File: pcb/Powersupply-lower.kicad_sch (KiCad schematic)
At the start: 0 parts

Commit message: pcp lower switcher made & implemented
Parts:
- added U3: TPS54294PWP, PWP16_2P31X2P46, symbol TPS54294:TPS54294PWP
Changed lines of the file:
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@@
 	(generator_version "10.0")
 	(paper "A4")
+	(symbol
+		(lib_id "TPS54294:TPS54294PWP")
+		(at 97.79 123.19 0)
+		(unit 1)
+		(body_style 1)
+		(exclude_from_sim no)
+		(in_bom yes)
+		(on_board yes)
+		(in_pos_files yes)
+		(dnp no)
+		(fields_autoplaced yes)
+		(property "Reference" "U3"
+			(at 139.7 62.23 0)
+			(show_name no)
+			(do_not_autoplace no)
+			(effects
+				(font
+					(size 1.524 1.524)
+				)
+			)
+		)
+		(property "Value" "TPS54294PWP"
+			(at 139.7 64.77 0)
+			(show_name no)
+			(do_not_autoplace no)
+			(effects
+				(font
+					(size 1.524 1.524)
+				)
+			)
+		)
+		(property "Footprint" "PWP16_2P31X2P46"
+			(at 138.684 100.584 0)
+			(hide yes)
+			(show_name no)
+			(do_not_autoplace no)
+			(effects
+				(font
+					(size 1.27 1.27)
+					(italic yes)
+				)
+			)
+		)
+		(property "Datasheet" "https://www.ti.com/lit/gpn/tps54294"
+			(at 138.43 96.774 0)
+			(hide yes)
+			(show_name no)
+			(do_not_autoplace no)
+			(effects
+				(font
+					(size 1.27 1.27)
+					(italic yes)
+				)
+			)
+		)
+		(property "Description" ""
+			(at 97.79 123.19 0)
+			(hide yes)
+			(show_name no)
+			(do_not_autoplace no)
+			(effects
+				(font
+					(size 1.27 1.27)
+				)
+			)
+		)
+		(pin "11"
+		)
+		(pin "3"
+		)
+		(pin "7"
+		)
+		(pin "2"
+		)
+		(pin "5"
+		)
+		(pin "1"
+		)
+		(pin "4"
+		)
+		(pin "6"
+		)
+		(pin "10"
+		)
+		(pin "9"
+		)
+		(pin "8"
+		)
+		(pin "15"
+		)
+		(pin "12"
+		)
+		(pin "16"
+		)
+		(pin "13"
+		)
+		(pin "14"
+		)
+		(instances
+			(project "tdt4295"
+				(path "/603dd496-f9c4-4a31-9104-19eec41ebc98/634870db-7705-458e-b29f-8b3e7772e7aa/a39ac6f6-156d-4e0b-9cc4-d1c3d15eb944"
+					(reference "U3")
+					(unit 1)
+				)
+			)
+		)
+	)
 )

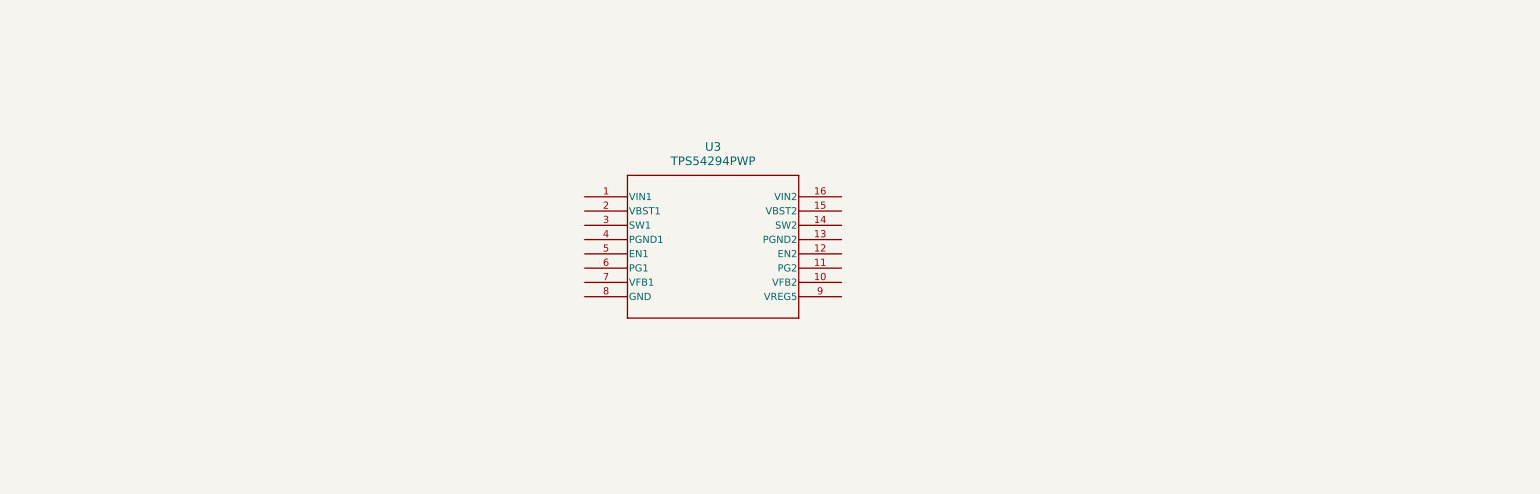
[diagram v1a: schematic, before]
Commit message: pcp lower made
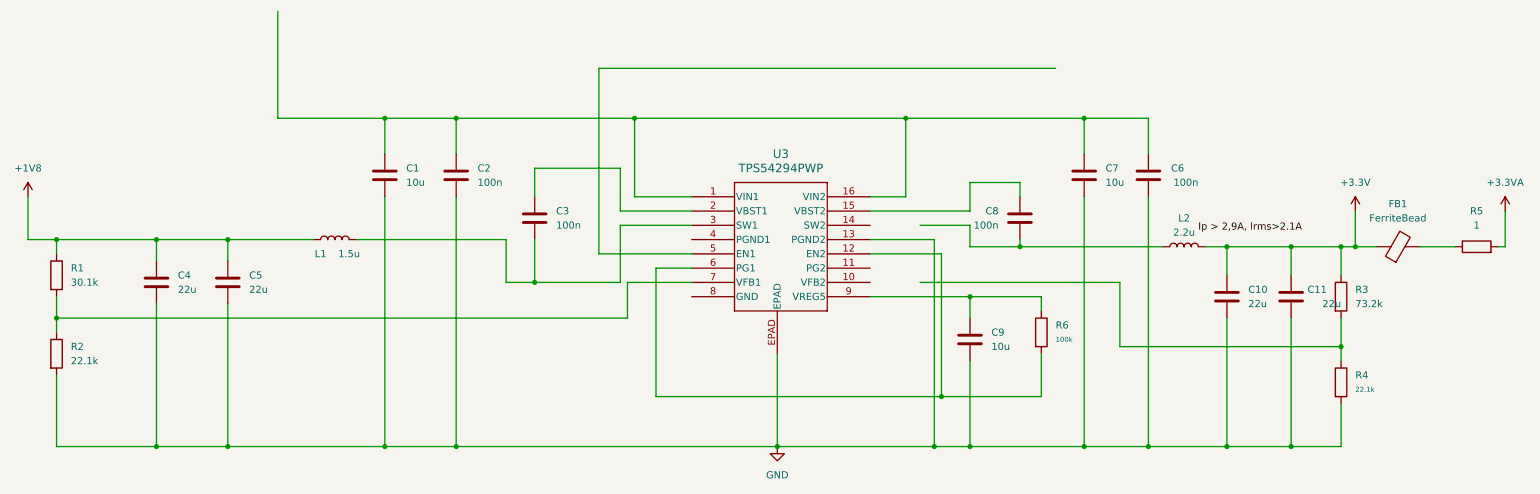
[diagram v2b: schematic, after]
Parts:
- removed U3: TPS54294PWP, PWP16_2P31X2P46, symbol TPS54294:TPS54294PWP
- added C1, C7, C9: 10u, symbol Device:C
- added C10, C11, C4, C5: 22u, symbol Device:C
- added C2, C3, C6, C8: 100n, symbol Device:C
- added FB1: FerriteBead, symbol Device:FerriteBead
- added L1: 1.5u, Relay_THT:Relay_DPDT_Kemet_EC2_NU_DoubleCoil, symbol Device:L
- added L2: 2.2u, Relay_THT:Relay_DPDT_Kemet_EC2_NU_DoubleCoil, symbol Device:L
- added R1: 30.1k, symbol Device:R
- added R2, R4: 22.1k, symbol Device:R
- added R3: 73.2k, symbol Device:R
- added R5: 1, symbol Device:R
- added R6: 100k, symbol Device:R
- added U3: TPS54294PWP, PWP16_2P31X2P46, symbol TPS54294PWP:TPS54294PWP
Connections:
- new net: FB1.2, R5.1
- new net: C1.1, C2.1, C6.1, C7.1, U3.1 (VIN1), U3.16 (VIN2)
- new net: C9.1, R6.1, U3.9 (VREG5)
- new net: R6.2, U3.12 (EN2), U3.6 (PG1)
- new net: R3.2, R4.1
- new net: R1.2, R2.1, U3.7 (VFB1)
- new net: C3.1, U3.2 (VBST1)
- new net: C3.2, L1.2, U3.3 (SW1)
- new net: C8.1, U3.15 (VBST2)
- new net: C8.2, L2.1
- new net +1V8: C4.1, C5.1, L1.1, R1.1
- new net +3.3V: C10.1, C11.1, FB1.1, L2.2, R3.1
- new net +3.3VA: R5.2
- new net GND: C1.2, C10.2, C11.2, C2.2, C4.2, C5.2, C6.2, C7.2, C9.2, R2.2, R4.2, U3.13 (PGND2), U3.EPAD

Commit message: fixed unconnected wire and some readability
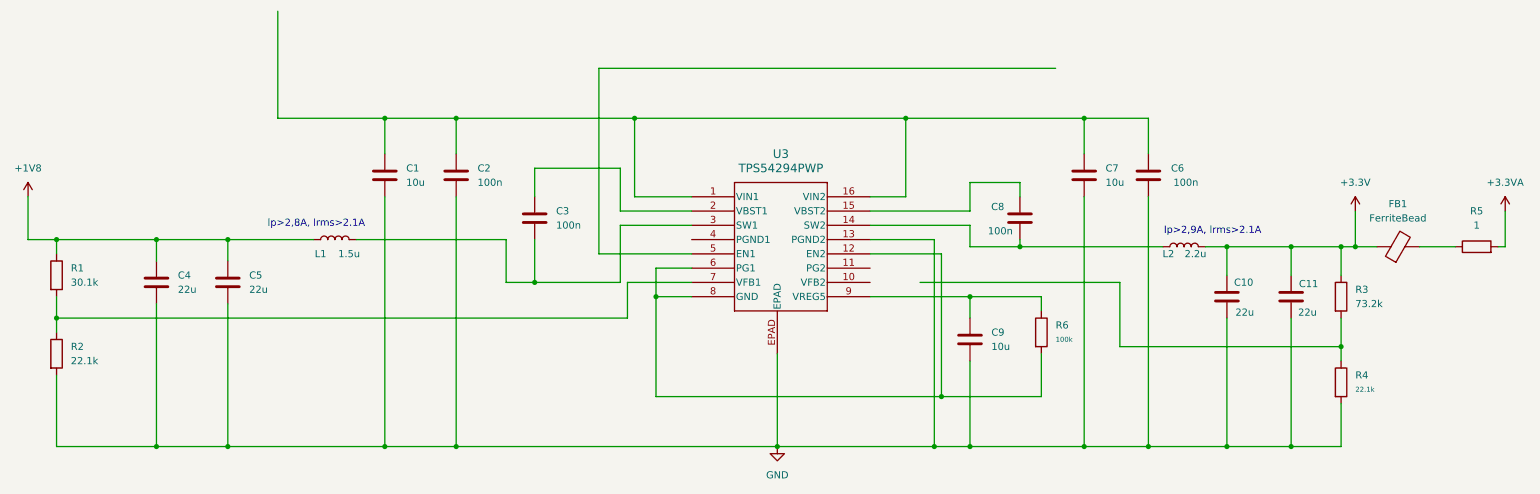
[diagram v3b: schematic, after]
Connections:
- net at R6.2, U3.12 (EN2), U3.6 (PG1): now also U3.8 (GND)
- net at C8.2, L2.1: now also U3.14 (SW2)
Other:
- note added: "lp>2,8A, lrms>2.1A"
- note added: "lp>2,9A, lrms>2.1A"
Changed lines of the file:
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@@
 	(generator_version "10.0")
 	(paper "A4")
+	(text "lp>2,9A, lrms>2.1A"
+		(exclude_from_sim no)
+		(at 228.6 77.216 0)
+		(effects
+			(font
+				(size 1.27 1.27)
+			)
+		)
+	)
+	(text "lp>2,8A, lrms>2.1A"
+		(exclude_from_sim no)
+		(at 69.088 75.946 0)
+		(effects
+			(font
+				(size 1.27 1.27)
+			)
+		)
+	)
 	(junction
 		(at 231.14 115.57)
@@
 	)
 	(junction
+		(at 129.54 88.9)
+		(diameter 0)
+		(color 0 0 0 0)
+	)
+	(junction
 		(at 251.46 80.01)
 		(diameter 0)
@@
 	(wire
 		(pts
-			(xy 176.53 76.2) (xy 185.42 76.2)
-		)
-		(stroke
-			(width 0)
-			(type default)
-		)
-	)
-	(wire
-		(pts
 			(xy 198.12 88.9) (xy 198.12 91.44)
 		)
@@
 	(wire
 		(pts
+			(xy 129.54 88.9) (xy 135.89 88.9)
+		)
+		(stroke
+			(width 0)
+			(type default)
+		)
+	)
+	(wire
+		(pts
 			(xy 22.86 115.57) (xy 40.64 115.57)
 		)
@@
 	(wire
 		(pts
-			(xy 129.54 83.82) (xy 129.54 106.68)
+			(xy 129.54 83.82) (xy 129.54 88.9)
 		)
 		(stroke
@@
 	(wire
 		(pts
+			(xy 129.54 88.9) (xy 129.54 106.68)
+		)
+		(stroke
+			(width 0)
+			(type default)
+		)
+	)
+	(wire
+		(pts
 			(xy 123.19 76.2) (xy 135.89 76.2)
 		)
@@
 	(wire
 		(pts
-			(xy 22.86 102.87) (xy 22.86 115.57)
+			(xy 167.64 76.2) (xy 185.42 76.2)
 		)
 		(stroke
@@
 		)
 	)
-	(label "lp > 2,9A, lrms>2.1A"
-		(at 226.06 77.47 0)
-		(effects
-			(font
-				(size 1.27 1.27)
-			)
-			(justify left bottom)
+	(wire
+		(pts
+			(xy 22.86 102.87) (xy 22.86 115.57)
+		)
+		(stroke
+			(width 0)
+			(type default)
 		)
 	)
@@
 		(in_pos_files yes)
 		(dnp no)
-		(fields_autoplaced yes)
 		(property "Reference" "C10"
-			(at 234.95 87.6299 0)
+			(at 232.41 86.36 0)
 			(show_name no)
 			(do_not_autoplace no)
@@
 		)
 		(property "Value" "22u"
-			(at 234.95 90.1699 0)
+			(at 232.664 91.694 0)
 			(show_name no)
 			(do_not_autoplace no)
@@
 		(in_pos_files yes)
 		(dnp no)
-		(fields_autoplaced yes)
 		(property "Reference" "C8"
-			(at 190.5 73.6599 0)
+			(at 191.516 72.898 0)
 			(show_name no)
 			(do_not_autoplace no)
@@
 		)
 		(property "Value" "100n"
-			(at 190.5 76.1999 0)
+			(at 193.04 77.216 0)
 			(show_name no)
 			(do_not_autoplace no)
@@
 		(dnp no)
 		(property "Reference" "C11"
-			(at 248.92 87.63 0)
+			(at 247.396 86.614 0)
 			(show_name no)
 			(do_not_autoplace no)
@@
 		)
 		(property "Value" "22u"
-			(at 251.46 90.17 0)
+			(at 247.142 91.694 0)
 			(show_name no)
 			(do_not_autoplace no)
@@
 		(in_pos_files yes)
 		(dnp no)
-		(fields_autoplaced yes)
 		(property "Reference" "L2"
-			(at 223.52 74.93 90)
+			(at 220.726 81.28 90)
 			(show_name no)
 			(do_not_autoplace no)
@@
 		)
 		(property "Value" "2.2u"
-			(at 223.52 77.47 90)
+			(at 225.552 81.28 90)
 			(show_name no)
 			(do_not_autoplace no)

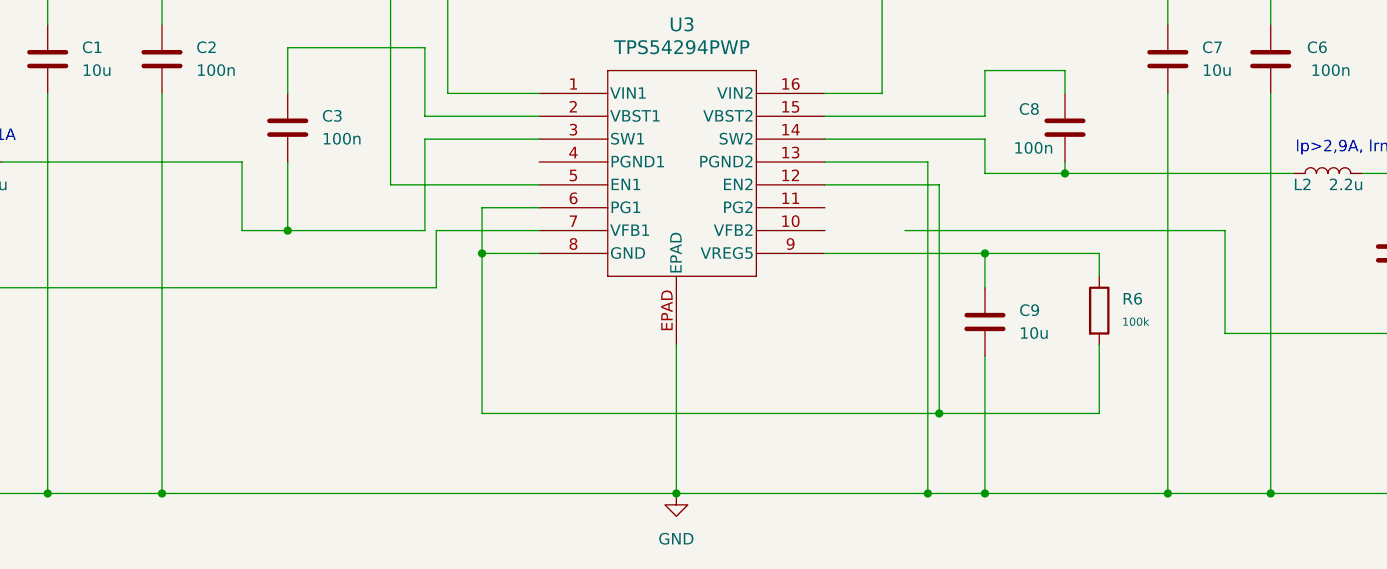
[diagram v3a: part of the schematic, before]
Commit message: (psp) fixed wrong wires
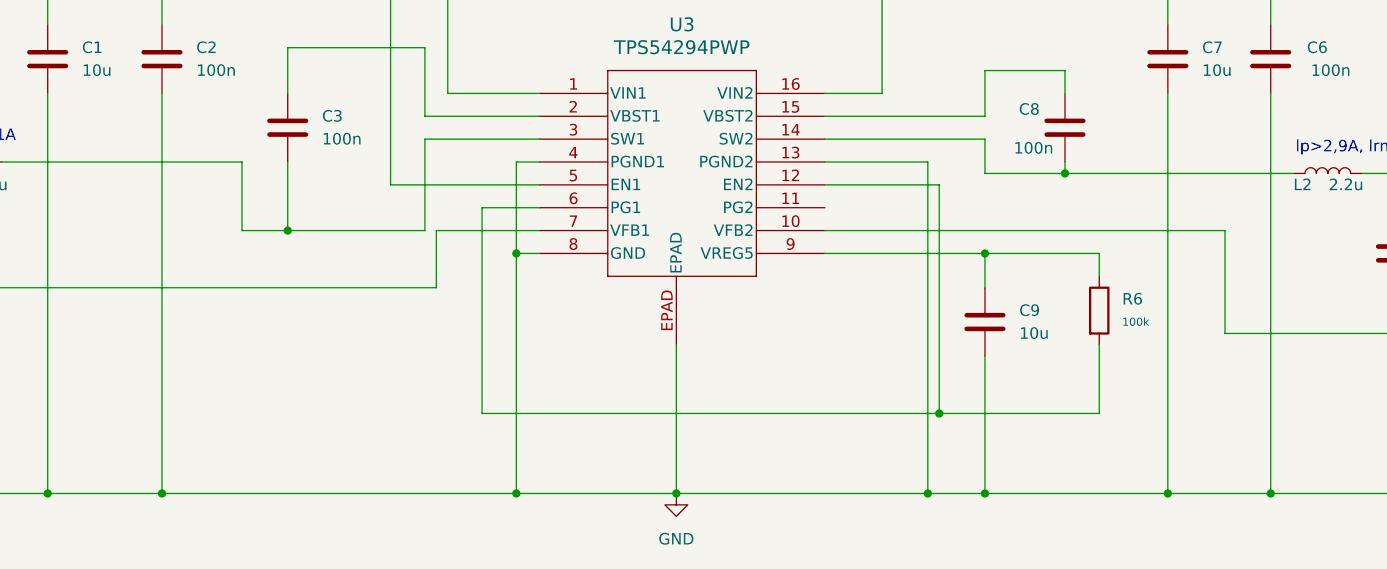
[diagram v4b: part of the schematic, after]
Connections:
- net GND: now also U3.4 (PGND1), U3.8 (GND)
- net at R6.2, U3.12 (EN2), U3.6 (PG1): no longer U3.8 (GND)
- net at R3.2, R4.1: now also U3.10 (VFB2)
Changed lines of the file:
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@@
+	)
+	(junction
+		(at 133.35 88.9)
+		(diameter 0)
+		(color 0 0 0 0)
 	)
 	(junction
@@
 	)
 	(junction
+		(at 133.35 115.57)
+		(diameter 0)
+		(color 0 0 0 0)
+	)
+	(junction
 		(at 125.73 57.15)
 		(diameter 0)
@@
 	)
 	(junction
-		(at 129.54 88.9)
-		(diameter 0)
-		(color 0 0 0 0)
-	)
-	(junction
 		(at 251.46 80.01)
 		(diameter 0)
@@
 	(wire
 		(pts
-			(xy 176.53 86.36) (xy 212.09 86.36)
-		)
-		(stroke
-			(width 0)
-			(type default)
-		)
-	)
-	(wire
-		(pts
 			(xy 167.64 81.28) (xy 180.34 81.28)
 		)
@@
 	(wire
 		(pts
-			(xy 135.89 83.82) (xy 129.54 83.82)
-		)
-		(stroke
-			(width 0)
-			(type default)
-		)
-	)
-	(wire
-		(pts
 			(xy 102.87 86.36) (xy 102.87 78.74)
 		)
@@
 	(wire
 		(pts
+			(xy 129.54 83.82) (xy 135.89 83.82)
+		)
+		(stroke
+			(width 0)
+			(type default)
+		)
+	)
+	(wire
+		(pts
 			(xy 93.98 71.12) (xy 93.98 115.57)
 		)
@@
 	(wire
 		(pts
-			(xy 129.54 88.9) (xy 135.89 88.9)
-		)
-		(stroke
-			(width 0)
-			(type default)
-		)
-	)
-	(wire
-		(pts
 			(xy 22.86 115.57) (xy 40.64 115.57)
 		)
@@
 	(wire
 		(pts
-			(xy 129.54 83.82) (xy 129.54 88.9)
+			(xy 133.35 115.57) (xy 151.13 115.57)
+		)
+		(stroke
+			(width 0)
+			(type default)
+		)
+	)
+	(wire
+		(pts
+			(xy 167.64 86.36) (xy 212.09 86.36)
+		)
+		(stroke
+			(width 0)
+			(type default)
+		)
+	)
+	(wire
+		(pts
+			(xy 129.54 83.82) (xy 129.54 106.68)
 		)
 		(stroke
@@
 	(wire
 		(pts
+			(xy 133.35 88.9) (xy 133.35 115.57)
+		)
+		(stroke
+			(width 0)
+			(type default)
+		)
+	)
+	(wire
+		(pts
 			(xy 251.46 92.71) (xy 251.46 97.79)
 		)
@@
 	(wire
 		(pts
-			(xy 129.54 88.9) (xy 129.54 106.68)
+			(xy 133.35 78.74) (xy 133.35 88.9)
 		)
 		(stroke
@@
 	(wire
 		(pts
+			(xy 135.89 78.74) (xy 133.35 78.74)
+		)
+		(stroke
+			(width 0)
+			(type default)
+		)
+	)
+	(wire
+		(pts
 			(xy 40.64 115.57) (xy 53.34 115.57)
 		)
@@
 	(wire
 		(pts
-			(xy 93.98 115.57) (xy 151.13 115.57)
+			(xy 93.98 115.57) (xy 133.35 115.57)
 		)
 		(stroke
@@
 		)
 		(stroke
+			(width 0)
+			(type default)
+		)
+	)
+	(wire
+		(pts
+			(xy 133.35 88.9) (xy 135.89 88.9)
+		)
+		(stroke

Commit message: (psp) added text notes for resistors
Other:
- note added: "1%"
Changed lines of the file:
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@@
 	(generator_version "10.0")
 	(paper "A4")
+	(text "1%\n"
+		(exclude_from_sim no)
+		(at 20.32 85.09 90)
+		(effects
+			(font
+				(size 1.27 1.27)
+			)
+		)
+	)
+	(text "1%\n"
+		(exclude_from_sim no)
+		(at 248.92 104.394 90)
+		(effects
+			(font
+				(size 1.27 1.27)
+			)
+		)
+	)
 	(text "lp>2,9A, lrms>2.1A"
 		(exclude_from_sim no)
 		(at 228.6 77.216 0)
+		(effects
+			(font
+				(size 1.27 1.27)
+			)
+		)
+	)
+	(text "1%\n"
+		(exclude_from_sim no)
+		(at 20.32 99.568 90)
 		(effects
 			(font
@@
 		(effects
 			(font
+				(size 1.27 1.27)
+			)
+		)
+	)
+	(text "1%\n"
+		(exclude_from_sim no)
+		(at 249.428 89.154 90)
+		(effects
+			(font
